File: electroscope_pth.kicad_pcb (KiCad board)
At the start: 2 copper layers, 21.3 x 45.7 mm, 17 parts, among them Q1 Q_PNP_EBC, Q2 Q_NPN_EBC, Q3 Q_PNP_EBC, Q4 Q_NPN_EBC, Q5 Q_PNP_EBC, Q6 Q_NPN_EBC, U1 ANT, U2 ANT

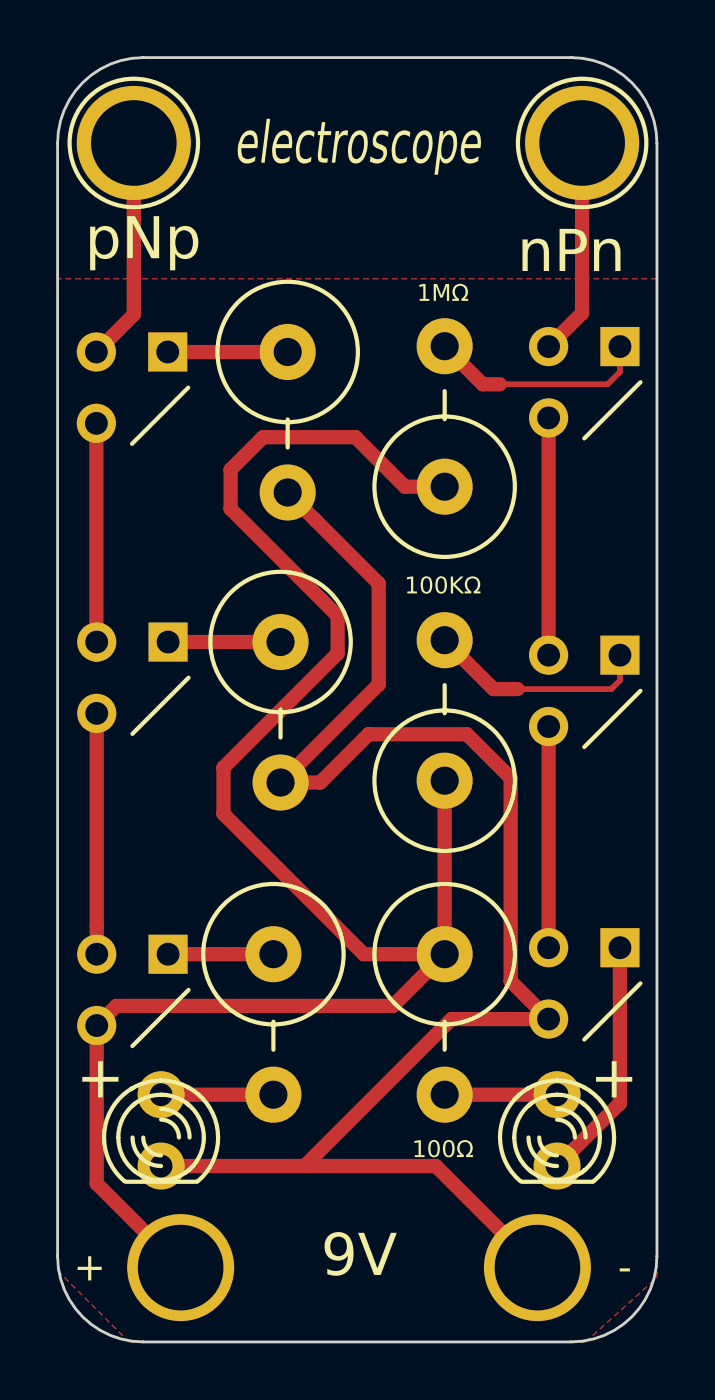
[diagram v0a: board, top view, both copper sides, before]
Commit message: electroscope: silkscreen improvements
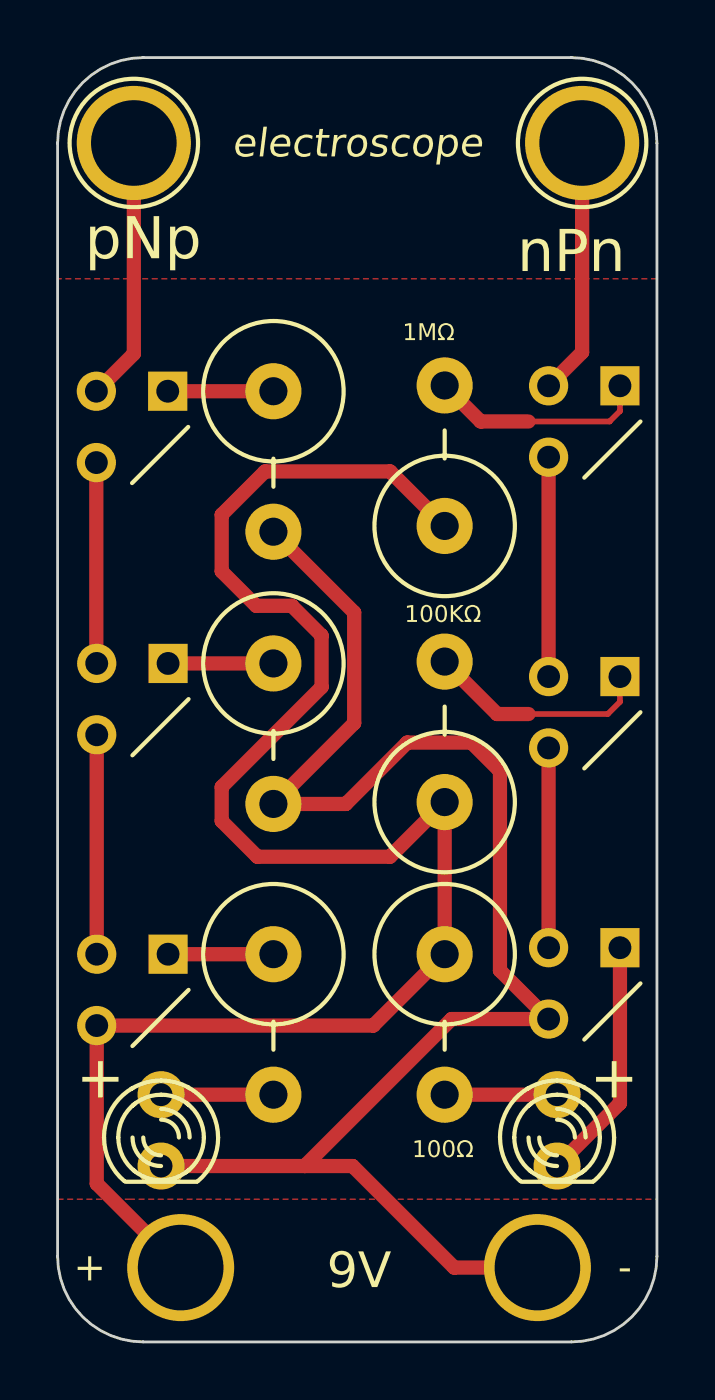
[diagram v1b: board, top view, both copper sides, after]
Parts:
- moved R5 1.49 mm to (136.7, 82.7)
- moved Q2 1.40 mm to (147.8, 81.3)
- moved R2 1.40 mm to (142.8, 82.5)
- moved Q5 1.40 mm to (131.7, 81.5)
- moved R3 0.80 mm to (136.7, 92.4)
- moved Q3 0.76 mm to (131.7, 91.2)
- moved Q4 0.76 mm to (147.8, 91.6)
- moved R4 0.76 mm to (142.8, 92.3)
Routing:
- net VCC: track 63.8 -> 61.9 mm
- net Net-(Q3-Pad2): track 8.26 -> 7.16 mm
- net Net-(Q5-Pad2): track 8.49 -> 9.39 mm
- net Net-(Q2-Pad2): track 8.24 -> 9.14 mm
- net GND: track 57.6 -> 56.8 mm
- net Net-(Q4-Pad1): track 7.87 -> 7.11 mm
- net Net-(Q1-Pad2): track 8.57 -> 7.81 mm
- net Net-(Q2-Pad1): track 8.45 -> 7.81 mm
- net Net-(Q5-Pad3): track 4.27 -> 3.76 mm
